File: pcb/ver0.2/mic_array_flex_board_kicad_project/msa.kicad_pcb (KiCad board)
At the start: 2 copper layers, 210 x 4.3 mm, 24 parts, among them U2 MP23DB01HPTR, U5 MP23DB01HPTR, U6 MP23DB01HPTR, U7 MP23DB01HPTR

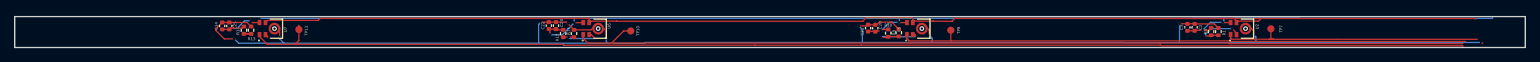
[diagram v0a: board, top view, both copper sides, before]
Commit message: make slim stack connector PLUG footprint + symbol, add slim stack connector to flex pcb
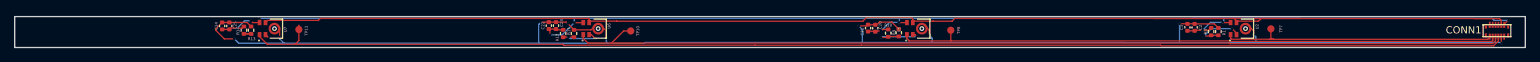
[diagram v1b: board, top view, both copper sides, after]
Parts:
- added CONN1: slim_stack_12pos_5035521222_schematic, OpenSourceSmartGlasses:slim_stack_molex_PLUG_5035521222, F.Cu at (226.1, 91.6)
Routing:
- net /MIC_DOUT_3: track 170.4 -> 176.1 mm
- net /MIC_DOUT_2: track 126.6 -> 131.7 mm
- net /MIC_DOUT_1: track 79.9 -> 84.2 mm
- net /MIC_CLK: track 185.9 -> 190.0 mm
- net GND: track 239.0 -> 243.0 mm, vias 9 -> 10
- net +3V3: track 218.9 -> 222.0 mm, vias 9 -> 10
- net /MIC_DOUT_0: track 36.6 -> 38.5 mm

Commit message: finish implementing slim stacks, add stiffeners to flex pcb, run DRC and fix all issues on both boards
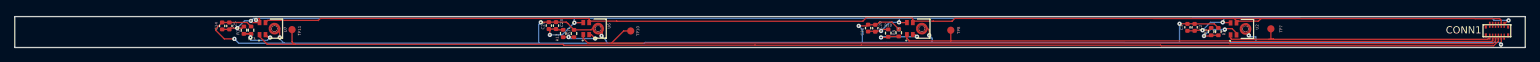
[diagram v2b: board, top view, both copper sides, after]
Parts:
- moved TP11 0.95 mm to (58.5, 91.5)
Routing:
- net Net-(R13-Pad2): track 1.79 -> 6.01 mm, vias 0 -> 2
- net +3V3: track 222.0 -> 224.0 mm
- net GND: track 243.0 -> 244.1 mm, vias 10 -> 9
- net /MIC_CLK: track 190.0 -> 190.7 mm
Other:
- board text added: "Stiffener"

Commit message: last changes setup for manufacturing for v0p2 - only step left is spacing of microphones
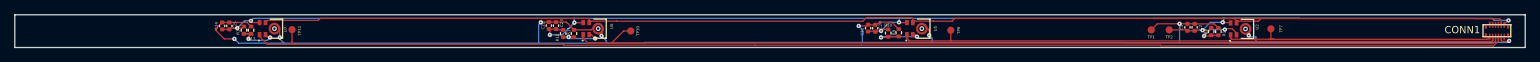
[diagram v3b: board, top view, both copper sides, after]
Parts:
- added TP1: TestPoint, mico:SMD_1x01_P1.27mm, F.Cu at (178.0, 91.5)
- added TP2: TestPoint, mico:SMD_1x01_P1.27mm, F.Cu at (180.5, 91.5)
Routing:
- net GND: track 244.1 -> 249.8 mm
- net +3V3: track 224.0 -> 225.4 mm, vias 10 -> 9
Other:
- board size 210 x 4.3 mm -> 210 x 4.5 mm

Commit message: change usb to proper right angle, set 45 mm spacing of microphones and proper overhang space
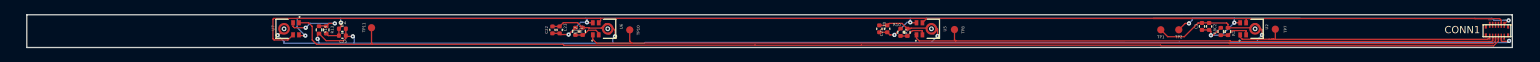
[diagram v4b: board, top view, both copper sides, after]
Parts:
- moved C24 16.7 mm to (65.5, 91.3), turned to 180 degrees
- moved TP11 16.1 mm to (74.6, 91.2)
- moved C25 15.8 mm to (65.5, 92.3), turned to 180 degrees
- moved R13 11.4 mm to (63.3, 91.5), turned to 90 degrees
- moved R14 9.44 mm to (62.3, 91.5), turned to -90 degrees
- moved TP8 5.51 mm to (155.7, 91.5)
- moved TP10 4.87 mm to (110.5, 91.5)
- moved C21 2.67 mm to (141.3, 91.3)
- moved C2 2.02 mm to (186.1, 91.0)
- moved C3 2.02 mm to (185.1, 91.0)
- moved R11 1.73 mm to (98.0, 91.7)
- moved R9 1.72 mm to (143.2, 91.8)
- moved U7 1.33 mm to (57.4, 91.3), turned to -90 degrees
- moved U5 1.33 mm to (147.4, 91.3)
- moved U6 1.33 mm to (102.4, 91.3)
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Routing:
- net GND: track 249.8 -> 241.3 mm, vias 9 -> 7
- net Net-(R10-Pad1): track 8.26 -> 3.93 mm, vias 2 -> 0
- net +3V3: track 225.4 -> 221.1 mm, vias 9 -> 10
- net /MIC_DOUT_3: track 176.1 -> 172.3 mm
- net Net-(R1-Pad2): track 7.56 -> 4.35 mm, vias 2 -> 0
- net Net-(R13-Pad2): track 6.30 -> 9.02 mm
- net /MIC_DOUT_2: track 131.7 -> 129.0 mm
- net Net-(R11-Pad2): track 6.36 -> 3.92 mm, vias 2 -> 0
- net /MIC_DOUT_0: track 38.5 -> 37.0 mm
- net /MIC_DOUT_1: track 84.2 -> 83.0 mm
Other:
- board size 210 x 4.5 mm -> 206.5 x 4.6 mm
- board text added: "ss1"
- board text added: "ss12"
- board text added: "ss6"
- board text added: "ss7"

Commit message: latest working mic array
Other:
- board text added: "Fold here"
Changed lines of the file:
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@@
     )
     (pad_to_mask_clearance 0)
+    (grid_origin 190.5 91.3)
     (pcbplotparams
-      (layerselection 0x00010fc_ffffffff)
+      (layerselection 0x00410fc_ffffffff)
       (disableapertmacros false)
-      (usegerberextensions false)
+      (usegerberextensions true)
       (usegerberattributes true)
       (usegerberadvancedattributes true)
-      (creategerberjobfile true)
+      (creategerberjobfile false)
       (svguseinch false)
       (svgprecision 6)
@@
       (plotinvisibletext false)
       (sketchpadsonfab false)
-      (subtractmaskfromsilk false)
+      (subtractmaskfromsilk true)
       (outputformat 1)
       (mirror false)
-      (drillshape 1)
+      (drillshape 0)
       (scaleselection 1)
-      (outputdirectory "")
+      (outputdirectory "gerber/")
     )
   )
@@
     (property "Sheetname" "")
     (attr smd)
-    (fp_text reference "R10" (at 1.0505 -1.464) (layer "F.SilkS")
+    (fp_text reference "R10" (at 1.24 0.025) (layer "F.SilkS")
       (effects (font (size 0.4 0.4) (thickness 0.1)))
     )
@@
     (property "Sheetname" "")
     (attr smd)
-    (fp_text reference "R12" (at 0.1 -0.95 90) (layer "F.SilkS")
+    (fp_text reference "R12" (at 0.153641 0.725 90) (layer "F.SilkS")
       (effects (font (size 0.4 0.4) (thickness 0.1)))
     )
@@
     (property "Sheetname" "")
     (attr smd)
-    (fp_text reference "C3" (at 0 0.8 90) (layer "F.SilkS")
+    (fp_text reference "C3" (at 1.205 0.125 180) (layer "F.SilkS")
       (effects (font (size 0.4 0.4) (thickness 0.1)))
     )
@@
     (property "Sheetname" "")
     (attr smd)
-    (fp_text reference "R8" (at -0.01 -1.8 90) (layer "F.SilkS")
+    (fp_text reference "R8" (at 1.22402 -0.016479 180) (layer "F.SilkS")
       (effects (font (size 0.4 0.4) (thickness 0.1)))
     )
@@
     (property "Sheetname" "")
     (attr smd)
-    (fp_text reference "R11" (at -0.355 -0.786 90) (layer "F.SilkS")
+    (fp_text reference "R11" (at -0.475 0.9 90) (layer "F.SilkS")
       (effects (font (size 0.4 0.4) (thickness 0.1)))
     )
@@
     (property "Sheetname" "")
     (attr smd)
-    (fp_text reference "C2" (at 0 -0.8 90) (layer "F.SilkS")
+    (fp_text reference "C2" (at -0.62 -0.775 180) (layer "F.SilkS")
       (effects (font (size 0.4 0.4) (thickness 0.1)))
     )
@@
     (property "Sheetname" "")
     (attr smd)
-    (fp_text reference "C20" (at -0.42 -0.7 90) (layer "F.SilkS")
+    (fp_text reference "C20" (at -1.125 -0.025 180) (layer "F.SilkS")
       (effects (font (size 0.4 0.4) (thickness 0.1)))
     )
@@
     (property "Sheetname" "")
     (attr smd)
-    (fp_text reference "R9" (at -0.1 -0.8 90) (layer "F.SilkS")
+    (fp_text reference "R9" (at -0.505 0.75 90) (layer "F.SilkS")
       (effects (font (size 0.4 0.4) (thickness 0.1)))
     )
@@
     (property "Sheetname" "")
     (attr smd)
-    (fp_text reference "R14" (at -0.05 -0.9 90) (layer "F.SilkS")
+    (fp_text reference "R14" (at -0.025 0.775 90) (layer "F.SilkS")
       (effects (font (size 0.4 0.4) (thickness 0.1)))
     )
@@
     (property "Sheetname" "")
     (attr smd)
-    (fp_text reference "R1" (at 0.2605 -1.8 90) (layer "F.SilkS")
+    (fp_text reference "R1" (at -1.17402 0.016479 180) (layer "F.SilkS")
       (effects (font (size 0.4 0.4) (thickness 0.1)))
     )
@@
     (property "Sheetname" "")
     (attr smd)
-    (fp_text reference "C21" (at 0.5 0.8 90) (layer "F.SilkS")
+    (fp_text reference "C21" (at -1.125 -0.125 180) (layer "F.SilkS")
       (effects (font (size 0.4 0.4) (thickness 0.1)))
     )
@@
     )
   )
+  (gr_line (start 197.440479 89.75) (end 197.440479 93.75) (layer "F.SilkS") (width 0.15))
+  (gr_line (start 52.440479 93.65) (end 52.440479 89.65) (layer "F.SilkS") (width 0.15))
   (gr_line (start 228.2 89.395) (end 21.68 89.4) (layer "Edge.Cuts") (width 0.1))
   (gr_line (start 21.68 93.95) (end 228.2 93.945) (layer "Edge.Cuts") (width 0.1))
   (gr_line (start 228.2 89.395) (end 228.2 93.945) (layer "Edge.Cuts") (width 0.1))
   (gr_line (start 21.68 89.4) (end 21.68 93.95) (layer "Edge.Cuts") (width 0.1))
-  (gr_circle (center 146.11 91.31) (end 146.49 90.83) (layer "User.1") (width 0.15) (fill none))
   (gr_rect (start 94 89.675) (end 103.975 92.95) (layer "User.1") (width 0.15) (fill none))
   (gr_rect (start 184.41 89.75) (end 193.855 92.885) (layer "User.1") (width 0.15) (fill none))
-  (gr_circle (center 191.12 91.36) (end 191.69 91.11) (layer "User.1") (width 0.15) (fill none))
   (gr_rect (start 67.4375 93.185) (end 55.6625 89.6) (layer "User.1") (width 0.15) (fill none))
   (gr_rect (start 223.86 89.755) (end 228.23 93.425) (layer "User.1") (width 0.15) (fill none))
-  (gr_circle (center 101.12 91.31) (end 101.61 90.83) (layer "User.1") (width 0.15) (fill none))
   (gr_rect (start 139.56 89.715) (end 148.835 92.92) (layer "User.1") (width 0.15) (fill none))
   (gr_text "ss1" (at 225.1 90.1) (layer "F.SilkS")
@@
     (effects (font (size 0.2 0.2) (thickness 0.05)))
   )
+  (gr_text "Fold here" (at 52.025 91.625 270) (layer "F.SilkS")
+    (effects (font (size 0.3 0.3) (thickness 0.07)))
+  )
   (gr_text "ss7" (at 225.05 93.15) (layer "F.SilkS")
     (effects (font (size 0.2 0.2) (thickness 0.05)))
+  )
+  (gr_text "Fold here" (at 197.85 91.575 90) (layer "F.SilkS")
+    (effects (font (size 0.3 0.3) (thickness 0.07)))
   )
   (gr_text "ss6" (at 227.1 90.1) (layer "F.SilkS")
@@
   (segment (start 67.1995 93.3495) (end 103.1505 93.3495) (width 0.15) (layer "B.Cu") (net 1))
   (segment (start 199.536 93.2495) (end 223.636 93.2495) (width 0.15) (layer "B.Cu") (net 1))
-  (segment (start 181.852189 93.265689) (end 181.936 93.181878) (width 0.15) (layer "B.Cu") (net 1))
   (segment (start 62.2495 92.8995) (end 62.1 92.75) (width 0.15) (layer "B.Cu") (net 1))
   (segment (start 227.529502 93.2495) (end 227.75 93.029002) (width 0.15) (layer "B.Cu") (net 1))
